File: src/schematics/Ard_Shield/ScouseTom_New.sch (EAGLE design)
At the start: 64 parts, among them IC1 LM317MBDT, IC2 AD5280, J1 STIM OUT, J4 Stim out Brd, Q2 FDN304P, Q3 FDV303N, T1 BC817, U1 ADM3202ARUZ, U3 ADUM5402ARWZ, U4 ADUM1410ARWZ, U5 ADUM5000ARWZ, U7 ADUM1410ARWZ, X1 IND DSUB, X2 SW DSUB, X3 CS DSUB

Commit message: Final version sent to PCBTrain with BOM and P&P
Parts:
- removed C36, C38, C40: .1uF, resistor:C-EUC0805
- removed C37, C39, C41: 1uF, resistor:C-EUC0805
- removed J4: Stim out Brd, con-molex:22-27-2021-02
- removed R8: 5K1, resistor:R-EU_R0805
- removed R9: 3k, resistor:R-EU_R0805
- removed T1: BC817, transistor-npn:BC817-40SMD
- removed U7: ADUM1410ARWZ, ADI-Phase-2:ADUM1410ARWZ
- added C21, C28, C6: 10uF, resistor:C-EUC0805
- added C22, C9: 0.1uF, resistor:C-EUC0805
- added C27: 1uF, resistor:C-EUC0805
- added J2: STIM OUT, con-molex:22-05-7028-02
- added Q1: FDV303N, SparkFun-DiscreteSemi:MOSFET-NCHANNEL2N7002PW
- added R3: 470, resistor:R-EU_R0805
- added R4: 33k, resistor:R-EU_R0805
- added U2: ADM3202ARUZ, Analog Devices_By_element14_Batch_1:ADM3202ARUZ
- C1, C4: value 0.1uF -> 10nF
- C10, C34: value .1uF -> 0.1uF
- C11, C23, C8: value 10uF -> 0.1uF
- C13, C16, C2, C5: value 0.1uF -> .1uF
- C14: value 1uF -> 10uF
- C19: value 10uF -> .1uF
- C20: value 0.1uF -> 1uF
- C25: value 10nF -> .1uF
- C26: value .1uF -> 10nF
- C3: value 0.1uF -> 10uF
- C30: value 10uF -> 1uF
- C33: value 10nF -> 1uF
- C7: value 10nF -> 0.1uF
- J1: value STIM OUT -> Stim out Brd; device con-molex:22-05-7028-02 -> con-molex:22-27-2021-02
- JP2: value Ext Stim -> V_TRIG_SELECT; device pinhead:PINHD-1X2 -> pinhead:PINHD-1X3
- JP3: value IND_BK -> Ext Stim; device pinhead:PINHD-2X5 -> pinhead:PINHD-1X2
- JP4: value V_TRIG_SELECT -> BONUS_PINOUT; device pinhead:PINHD-1X3 -> pinhead:PINHD-1X5
- JP5: value BONUS_PINOUT -> IND_BK; device pinhead:PINHD-1X5 -> pinhead:PINHD-2X5
- Q2: value FDN304P -> BC817; device SparkFun-DiscreteSemi:MOSFET-PCHANNEL -> transistor-npn:BC817-40SMD
- Q3: value FDV303N -> FDN304P; device SparkFun-DiscreteSemi:MOSFET-NCHANNEL2N7002PW -> SparkFun-DiscreteSemi:MOSFET-PCHANNEL
- R6: value 470 -> 5K1
- R7: value 33k -> 3k
- U1: value ADM3202ARUZ -> ADUM5402ARWZ; device Analog Devices_By_element14_Batch_1:ADM3202ARUZ -> Analog Devices_By_element14_Batch_1:ADUM5402ARWZ
- U3: value ADUM5402ARWZ -> ADUM5000ARWZ; device Analog Devices_By_element14_Batch_1:ADUM5402ARWZ -> Analog Devices_By_element14_Batch_1:ADUM5000ARWZ
- U5: value ADUM5000ARWZ -> ADUM1410ARWZ; device Analog Devices_By_element14_Batch_1:ADUM5000ARWZ -> ADI-Phase-2:ADUM1410ARWZ
- renumbered C35 to C17, DIN8 to DIN1, DUE to ARD1, R10 to R5, R13 to R1, R14 to R2, V2 to V1, X1 to DSUB3, X2 to DSUB2, X3 to DSUB1
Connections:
- net +3V3: now also C4.1, C5.1, C6.1, U1.VDD1; no longer C26.1, C7.1, C8.1, U3.VDD1
- net +5V: now also C13.1, C15.1, C19.1, C20.1, C32.1, C33.1, U3.RCSEL, U3.VDD1, U3.VDD1_2; no longer C29.1, C30.1, C36.1, C37.1, C40.1, C41.1, U5.RCSEL, U5.VDD1_2, U7.VDD1
- net 5V_SIDE: now also C14.1, C18.2; no longer C20.2, C23.1
- net BONUS_1: now also JP4.1; no longer JP5.1
- net BONUS_2: now also JP4.2; no longer JP5.2
- net BONUS_3: now also JP4.3; no longer JP5.3
- net BONUS_4: now also JP4.4; no longer JP5.4
- net CS_EXTRA: now also U1.VIB; no longer U3.VIB
- net CS_EXTRA_ISO: now also U1.VOB; no longer U3.VOB
- net CS_PMARK: now also U1.VOD; no longer U3.VOD
- net CS_PMARK_ISO: now also U1.VID; no longer U3.VID
- net GND: now also C13.2, C20.2, C21.2, C22.1, C23.1, C27.1, C31.2, C32.2, C33.2, C34.1, C4.2, C5.2, C6.2, J2-2.S, JP3.2, JP4.5, Q1.S, Q2.E, R7.1, U1.GND1, U1.GND1_2, U3.NC_2, U3.RCIN; no longer C13.1, C14.1, C16.1, C18.1, C26.2, C29.2, C30.2, C36.2, C37.2, C40.2, C41.2, C7.2, C8.2, J4-2.S, JP2.2, JP5.5, Q3.S, R9.1, T1.E, U5.NC_2, U5.RCIN, U7.GND1, U7.GND1_2
- net GND_ISO_RS232: now also C1.2, C2.2, C3.2, C7.2, U1.GNDISO, U1.GND_ISO, U1.VSEL, U2.GND; no longer C24.2, C25.2, C4.2, C5.2, U1.GND, U3.GNDISO, U3.GND_ISO, U3.VSEL
- net GND_ISO_TRIG: now also C16.2, C24.2, C25.2, C26.2, C28.2, C29.2, C30.2, JP2.1, JP5.10, JP5.9, U3.GNDISO, U3.GNDISO_2, U3.NC, U3.NC_3, U3.NC_4, U5.CTRL2, U5.GND2, U5.GND2_2; no longer C11.2, C31.2, C32.2, C33.2, C34.2, C38.2, C39.2, JP3.10, JP3.9, JP4.1, U5.GNDISO, U5.GNDISO_2, U5.NC, U5.NC_3, U5.NC_4, U7.CTRL2, U7.GND2, U7.GND2_2
- net IND_EX_1: now also U5.VIB; no longer U7.VIB
- net IND_EX_1_ISO: now also JP5.3, U5.VOB; no longer JP3.3, U7.VOB
- net IND_EX_2: now also U5.VIC; no longer U7.VIC
- net IND_EX_2_ISO: now also JP5.2, U5.VOC; no longer JP3.2, U7.VOC
- net IND_EX_3: now also U5.VID; no longer U7.VID
- net IND_EX_3_ISO: now also JP5.1, U5.VOD; no longer JP3.1, U7.VOD
- net IND_FREQ: now also U5.VIA; no longer U7.VIA
- net IND_FREQ_ISO: now also JP5.4, U5.VOA; no longer JP3.4, U7.VOA
- net IND_START_ISO: now also JP5.6; no longer JP3.6
- net IND_STIM: now also JP3.1, R4.1; no longer JP2.1, R7.1
- net IND_STIM_ISO: now also JP5.7; no longer JP3.7
- net IND_STOP_ISO: now also JP5.5; no longer JP3.5
- net IND_SWITCH_ISO: now also JP5.8; no longer JP3.8
- net N$1: now also Q2.B, R4.2; no longer R7.2, T1.B
- net N$22: now also C8.2, U2.C1+; no longer C1.2, U1.C1+
- net N$23: now also C8.1, U2.C1-; no longer C1.1, U1.C1-
- net N$24: now also C9.2, U2.C2+; no longer C2.2, U1.C2+
- net N$25: now also C9.1, U2.C2-; no longer C2.1, U1.C2-
- net N$26: now also C11.2, U2.V+; no longer C3.2, U1.V+
- net N$27: now also C10.1, U2.V-; no longer C4.1, U1.V-
- net N$3: now also Q2.C, Q3.G, R6.2; no longer Q2.G, R8.2, T1.C
- net N$5: now also Q1.G; no longer Q3.G
- net POT_IN: now also R3.2; no longer R6.2
- net RS232_RXD: now also U2.T1OUT; no longer U1.T1OUT
- net RS232_TXD: now also U2.R1IN; no longer U1.R1IN
- net STIM_OUT: now also J2-1.S, Q3.D, R7.2; no longer J4-1.S, Q2.D, R9.2
- net STIM_REG_VIN-: now also C14.2, C18.1, Q1.D; no longer C20.1, C23.2, Q3.D
- net TRIG_DISABLE_2: now also U5.DISABLE; no longer U7.DISABLE
- net TTL_RX: now also U1.VOC; no longer U3.VOC
- net TTL_RX_ISO: now also U1.VIC, U2.R1OUT; no longer U1.R1OUT, U3.VIC
- net TTL_TX: now also U1.VIA; no longer U3.VIA
- net TTL_TX_ISO: now also U1.VOA, U2.T1IN; no longer U1.T1IN, U3.VOA
- net V_ISO_RS232: now also C1.1, C11.1, C2.1, C7.1, U1.VISO, U2.VCC; no longer C10.1, C24.1, C25.1, C5.1, U1.VCC, U3.VISO
- net V_ISO_TRIG: now also C16.1, C24.1, C25.1, C26.1, C28.1, C29.1, C30.1, JP2.3, U3.VISO, U3.VISO_2, U5.VDD2; no longer C11.1, C31.1, C32.1, C33.1, C34.1, C38.1, C39.1, JP4.3, U5.VISO, U5.VISO_2, U7.VDD2
- net V_SELECT: now also JP2.2, U3.VSEL; no longer JP4.2, U5.VSEL
- net V_STIM: now also C27.2, Q3.S, R3.1; no longer C14.2, Q2.S, R8.1
- net V_STIM_REF: now also C21.1, C22.2, C23.2, C31.1, C34.2; no longer C13.2, C15.1, C16.2, C18.2, C19.1
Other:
- moved on the sheet: C1, C10, C11, C13, C14, C15, C16, C18, C19, C2, C20, C23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

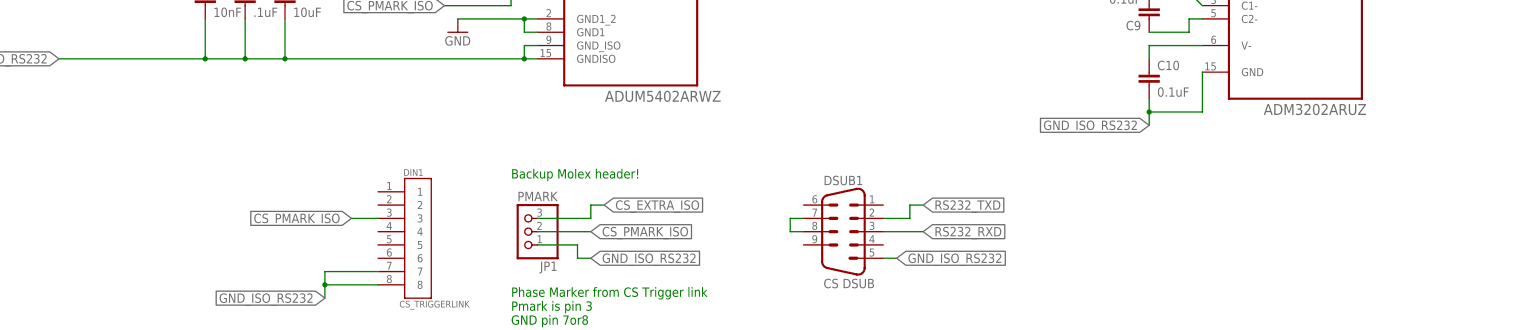
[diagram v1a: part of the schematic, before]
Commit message: CS extra pin added. Fixed angles on tracks
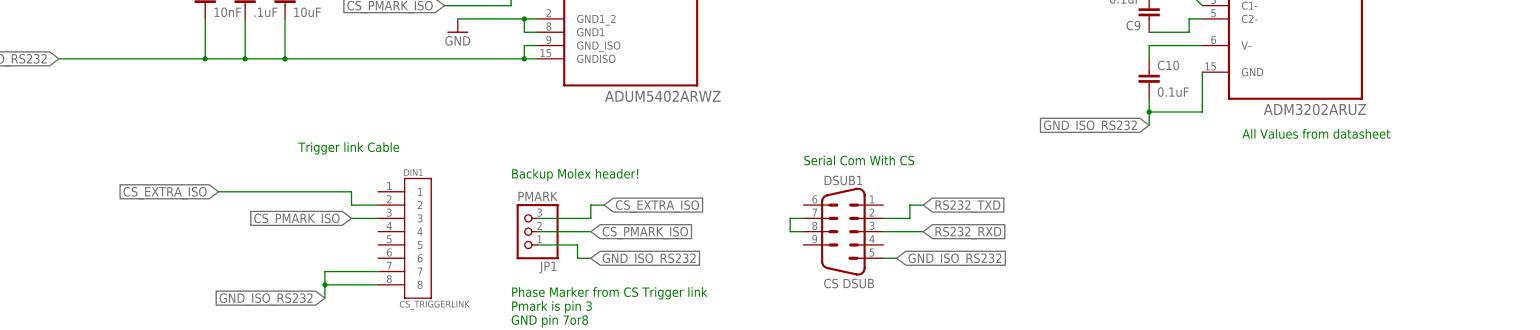
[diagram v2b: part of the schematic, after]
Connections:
- net CS_EXTRA_ISO: now also DIN1.2
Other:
- note added: "All Values from datasheet"
- note added: "Serial Com With CS"
- note added: "Trigger link Cable"
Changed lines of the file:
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@@
 <text x="373.38" y="-170.18" size="1.778" layer="91">DC DC Convertor for STIM, 12V</text>
 <text x="436.88" y="-96.52" size="1.778" layer="91">VOLTAGE ADJUSTMENT</text>
+<text x="-116.84" y="-20.32" size="1.778" layer="91">Trigger link Cable</text>
+<text x="-20.32" y="-22.86" size="1.778" layer="91">Serial Com With CS</text>
+<text x="63.5" y="-17.78" size="1.778" layer="91">All Values from datasheet</text>
 </plain>
 <instances>
@@
 <label x="-58.42" y="-30.48" size="1.778" layer="95" xref="yes"/>
 </segment>
-</net>
+<segment>
+<pinref part="DIN1" gate="G$1" pin="2"/>
+<wire x1="-101.6" y1="-30.48" x2="-106.68" y2="-30.48" width="0.1524" layer="91"/>
+<wire x1="-106.68" y1="-30.48" x2="-106.68" y2="-27.94" width="0.1524" layer="91"/>
+<wire x1="-106.68" y1="-27.94" x2="-132.08" y2="-27.94" width="0.1524" layer="91"/>
+<label x="-132.08" y="-27.94" size="1.778" layer="95" rot="R180" xref="yes"/>
+</segment>
+</net>

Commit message: Added pulldown resistors on CS and Switch board comm
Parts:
- added R10, R11, R8, R9: 10k, resistor:R-EU_R0805
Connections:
- net CS_EXTRA_ISO: now also R9.1
- net CS_PMARK_ISO: now also R8.2
- net GND: now also R10.1, R11.1
- net GND_ISO_RS232: now also R8.1, R9.2
- net TEST_1: now also R10.2
- net TEST_2: now also R11.2
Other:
- note added: "Extra pin breakouts. Useful in debugging. Bonus4 soimetimes used to check timings of ISRs"
